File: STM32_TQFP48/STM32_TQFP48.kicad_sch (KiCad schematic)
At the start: 37 parts, among them SW1 SW_Push, SW2 SW_Push, U1 STM32L010C6Tx

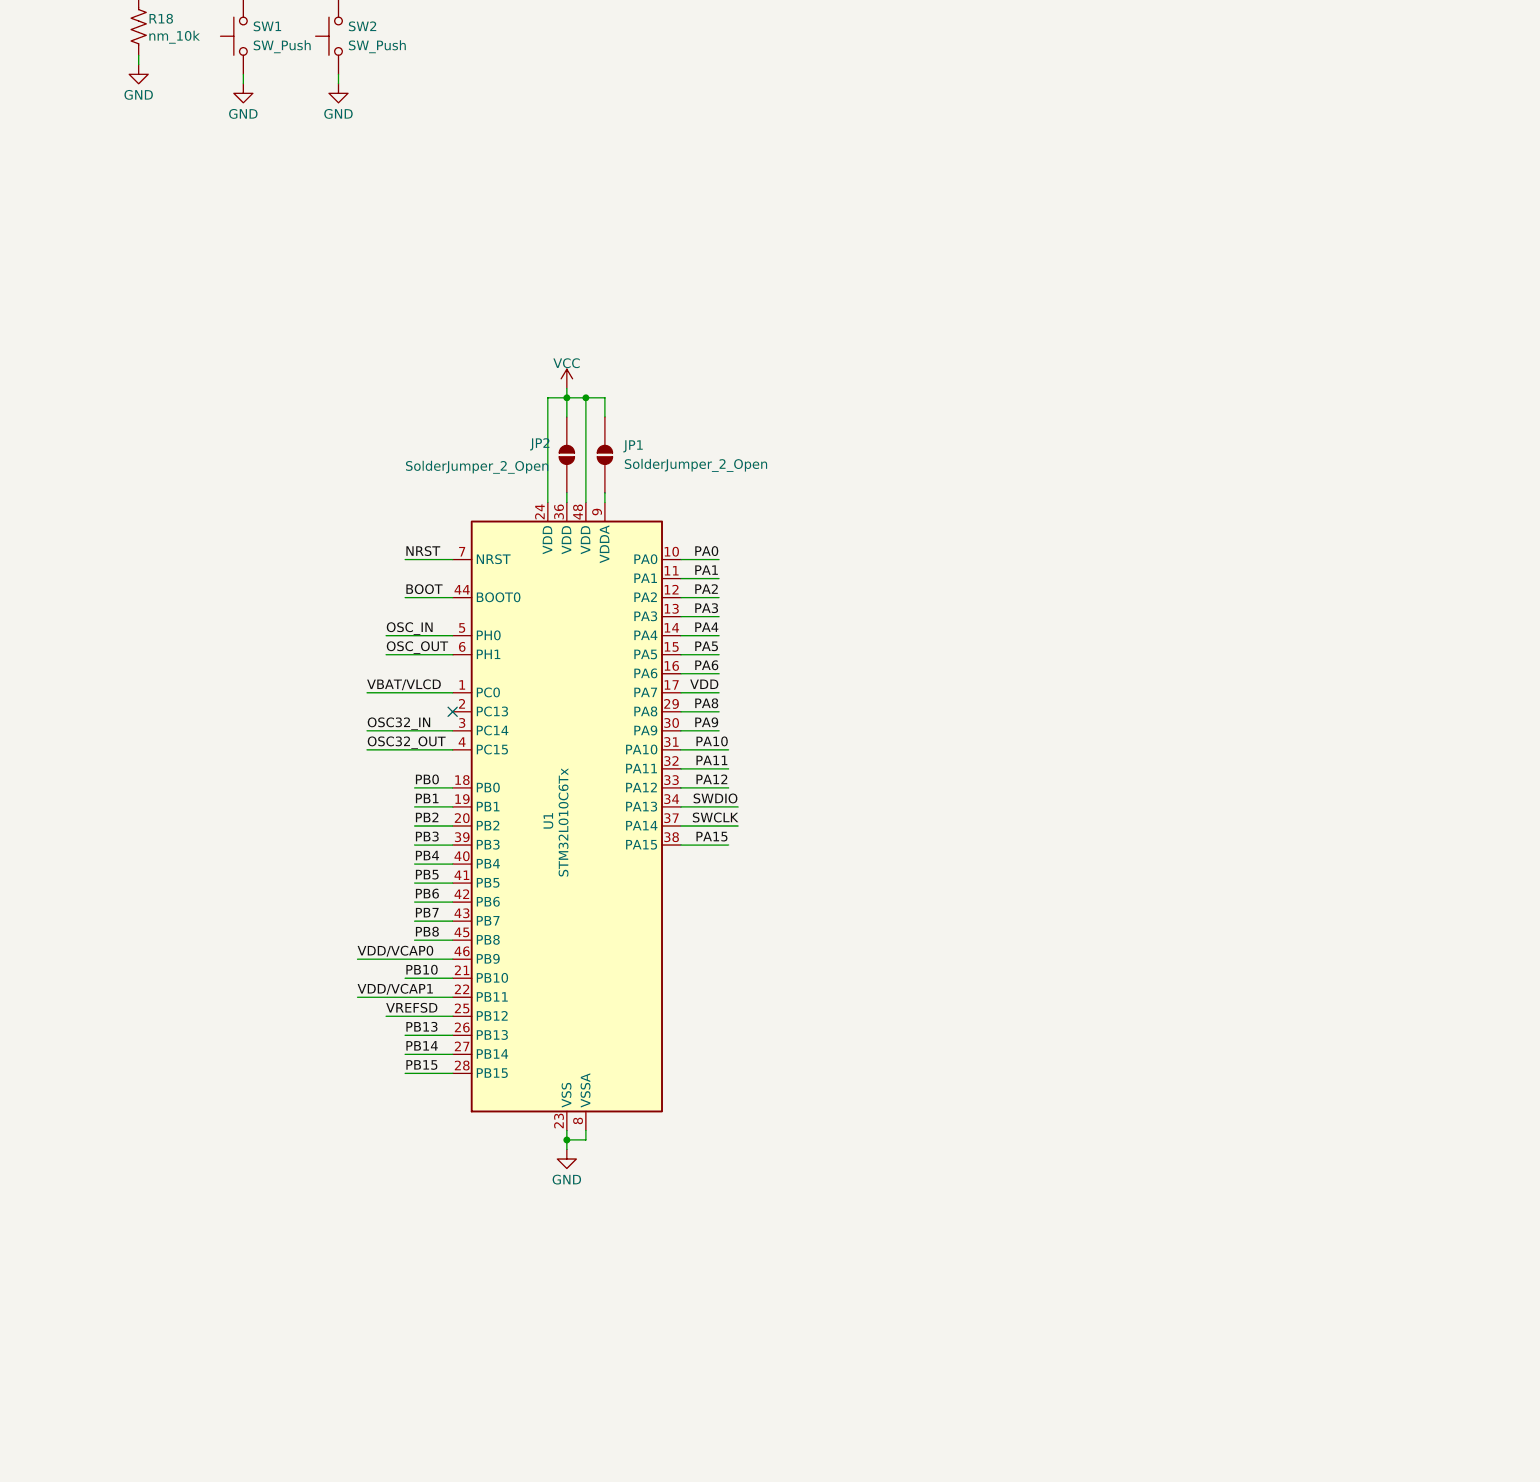
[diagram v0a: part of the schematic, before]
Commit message: STM32_TQFP48: Zaktualizowanie opisu konfiguracji pinoutu uC
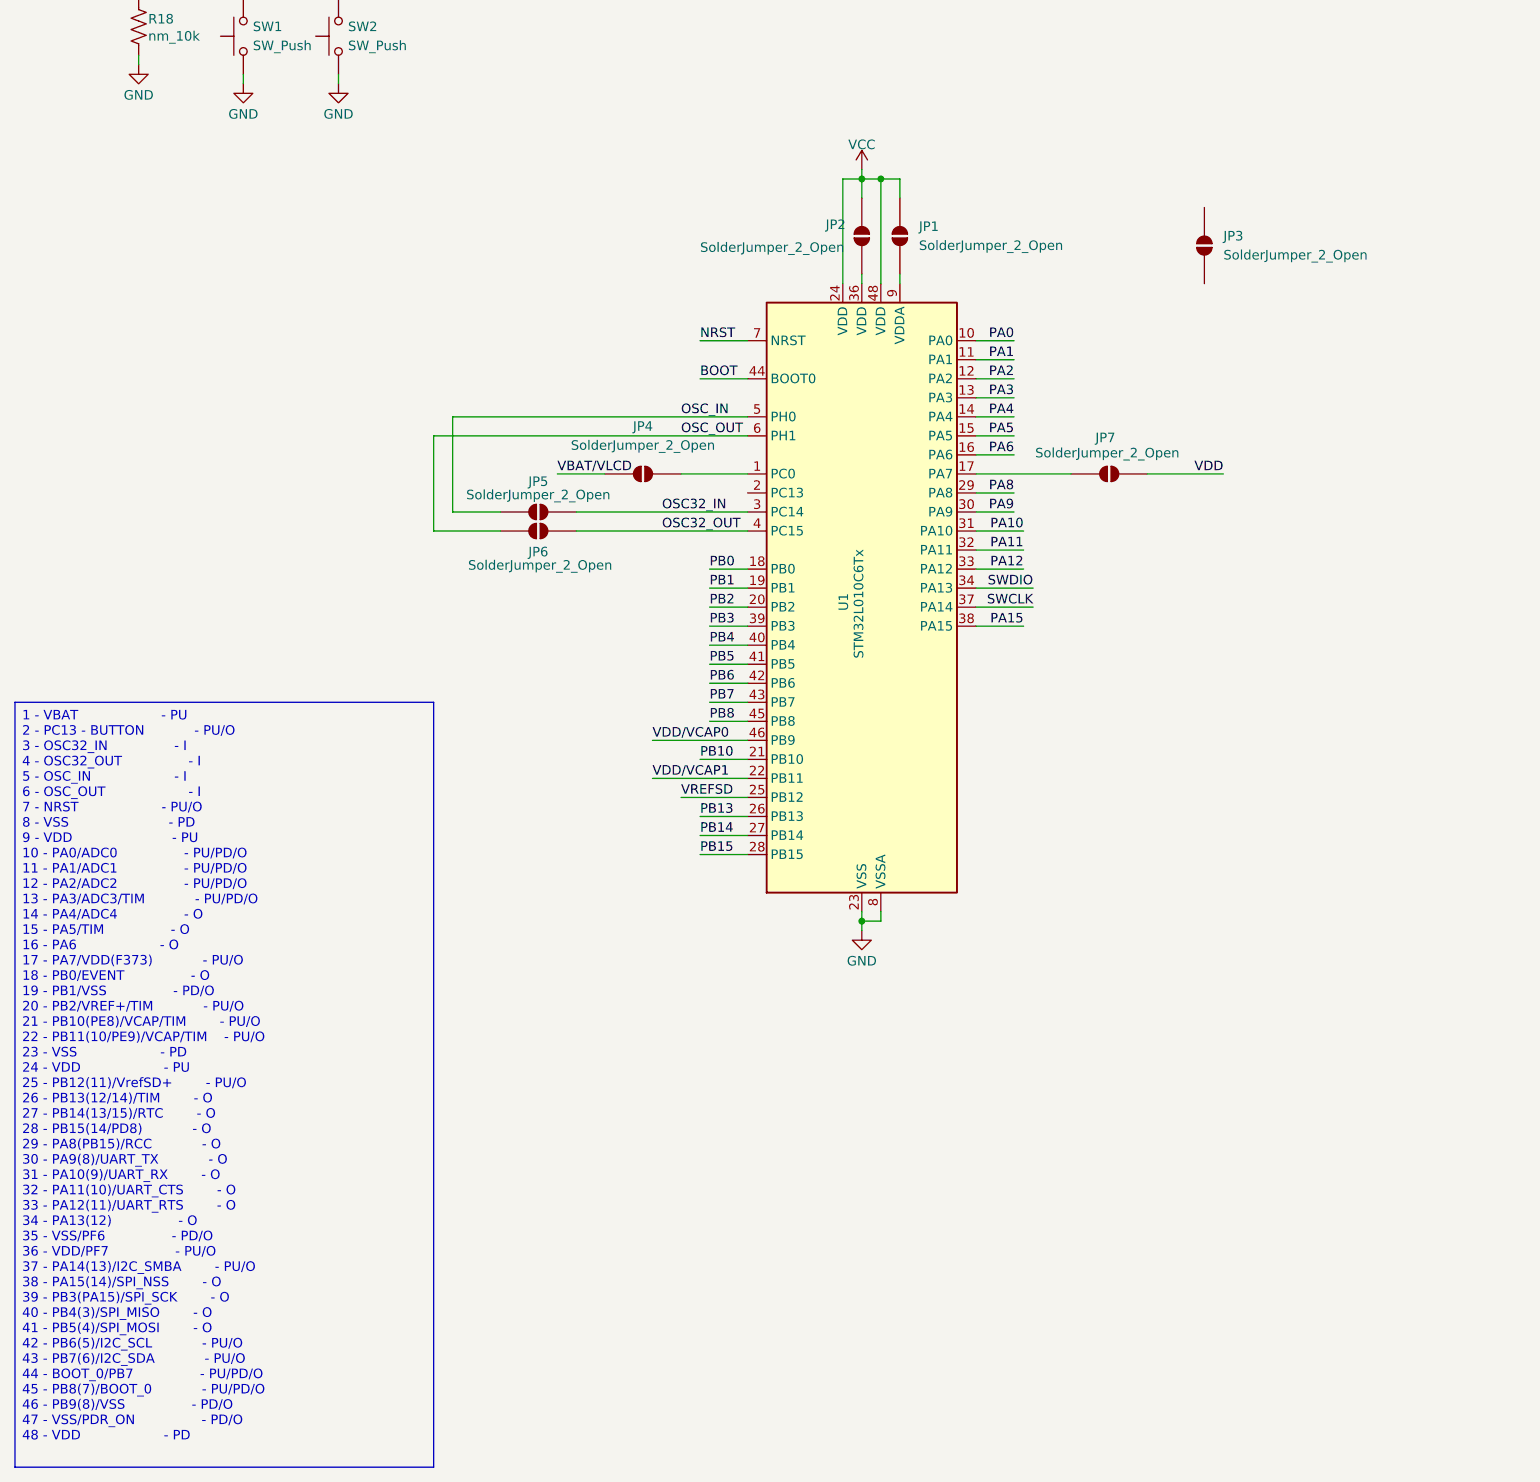
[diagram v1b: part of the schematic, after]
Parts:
- added JP3, JP4, JP5, JP6, JP7: SolderJumper_2_Open, symbol Jumper:SolderJumper_2_Open
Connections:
- net OSC32_IN: now also JP5.1 (A)
- net OSC32_OUT: now also JP6.1 (A)
- net OSC_IN: now also JP5.2 (B)
- net OSC_OUT: now also JP6.2 (B)
- net VBAT/VLCD: now also JP4.2 (B); no longer U1.1 (PC0)
- net VDD: now also JP7.1 (A); no longer U1.17 (PA7)
- new net: JP4.1 (A), U1.1 (PC0)
- new net: JP7.2 (B), U1.17 (PA7)
- no-connect marks 1 -> 0
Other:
- moved on the sheet: JP1, JP2, U1

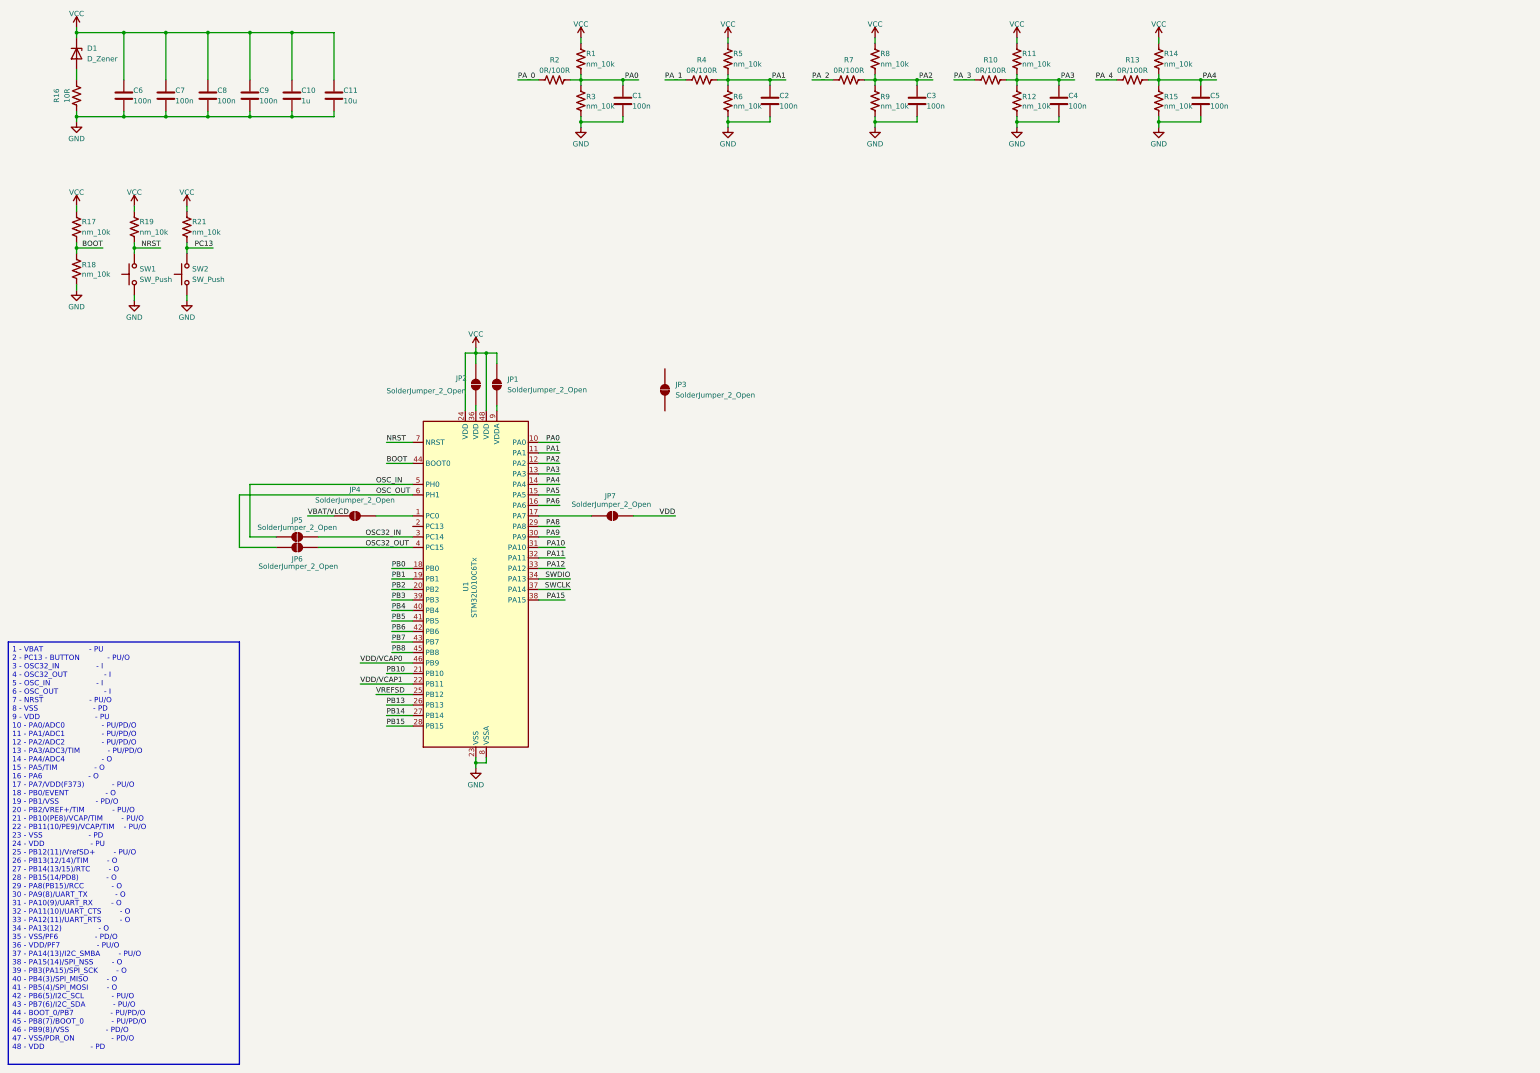
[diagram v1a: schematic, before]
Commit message: STM32_TQFP: Dalsza aktulizacja pinoutu, dodanie pierwszych układów wyprowadzeń.
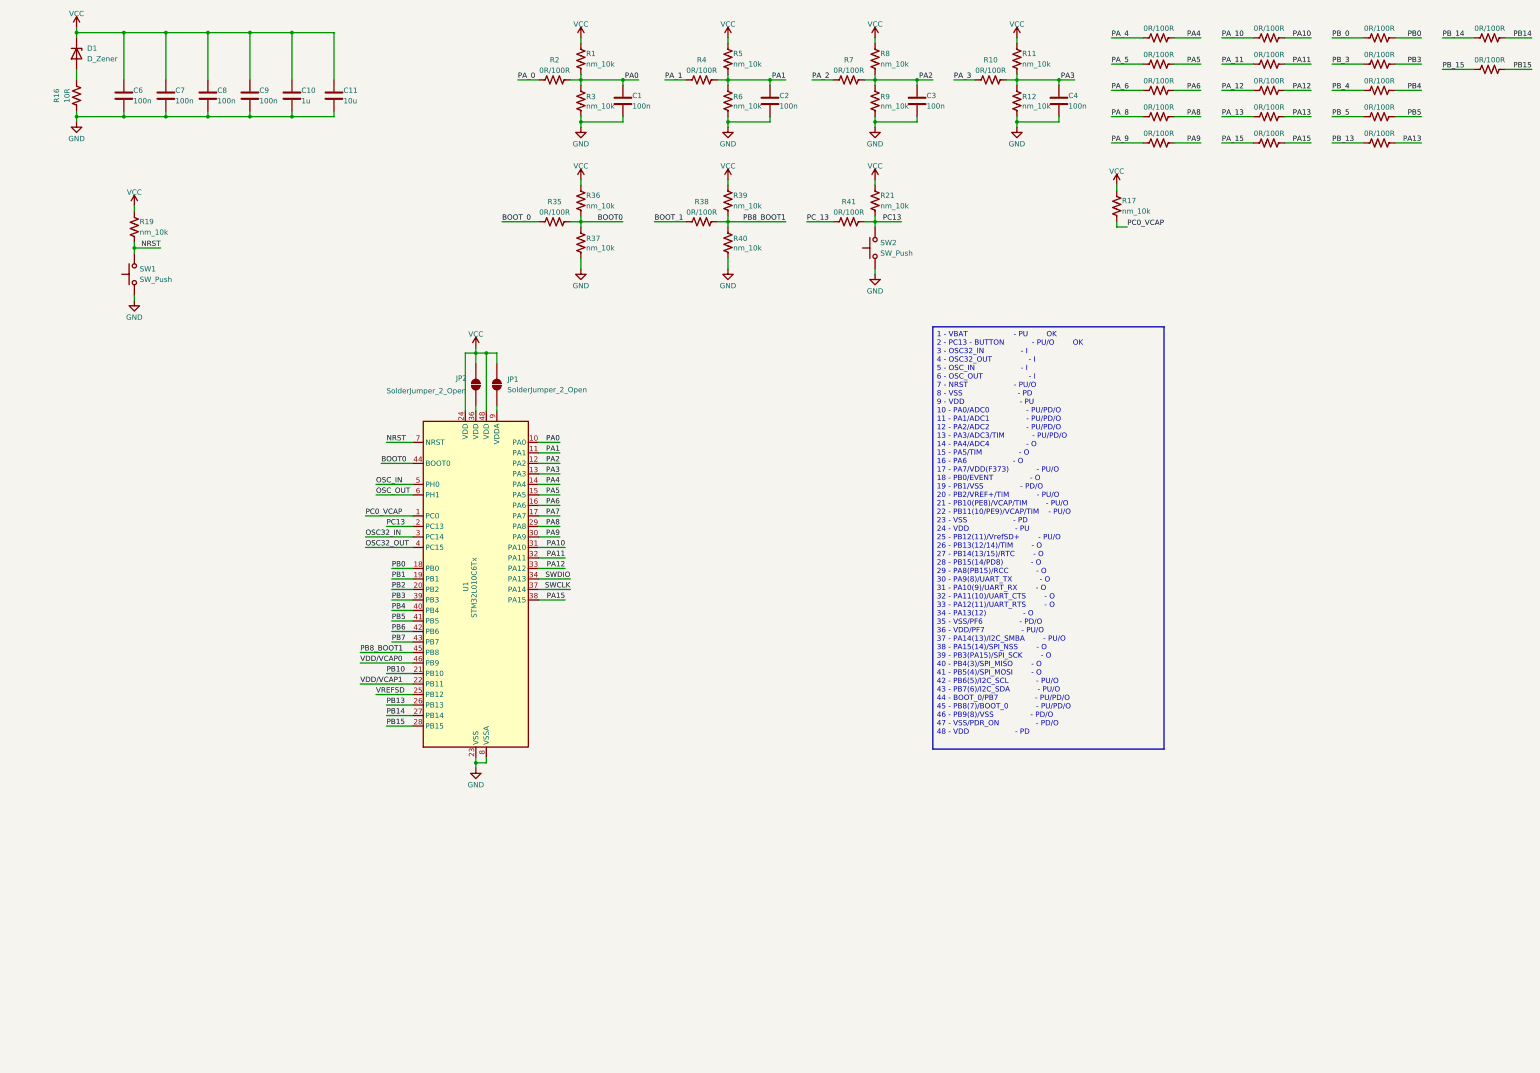
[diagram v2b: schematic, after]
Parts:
- removed C5: 100n, symbol Device:C
- removed JP3, JP4, JP5, JP6, JP7: SolderJumper_2_Open, symbol Jumper:SolderJumper_2_Open
- removed R18: nm_10k, symbol Device:R_US
- added R20, R22, R23, R24, R25, R26, R27, R28, R29, R30, R31, R32, R33, R34, R35, R38, R41: 0R/100R, symbol Device:R_US
- added R36, R37, R39, R40: nm_10k, symbol Device:R_US
- R14, R15: value nm_10k -> 0R/100R
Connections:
- net GND: now also R37.1, R40.1; no longer R15.1
- net PA10: now also R27.2
- net PA11: now also R28.2
- net PA12: now also R29.2
- net PA15: now also R31.2
- net PA4: no longer R14.2, R15.2
- net PA5: now also R14.2
- net PA6: now also R15.2
- net PA8: now also R25.2
- net PA9: now also R26.2
- net PB0: now also R20.2
- net PB14: now also R23.2
- net PB15: now also R24.2
- net PB3: now also R32.2
- net PB4: now also R33.2
- net PB5: now also R34.2
- net PC13: now also U1.2 (PC13), R41.2
- net VCC: now also R36.1, R39.1; no longer R14.1
- net PC0_VCAP: now reaches U1.1 (PC0)
- net PC0_VCAP: now also R17.2
- net PA7: now reaches U1.17 (PA7)
- net BOOT renamed BOOT0
- net BOOT0: now also R35.2, R36.2, R37.2; no longer R17.2
- net PB8 renamed PB8_BOOT1
- net PB8_BOOT1: now also R38.2, R39.2, R40.2
- new net BOOT_0: R35.1
- new net BOOT_1: R38.1
- new net PA13: R22.2, R30.2
- new net PA_10: R27.1
- new net PA_11: R28.1
- new net PA_12: R29.1
- new net PA_13: R30.1
- new net PA_15: R31.1
- new net PA_5: R14.1
- new net PA_6: R15.1
- new net PA_8: R25.1
- new net PA_9: R26.1
- new net PB_0: R20.1
- new net PB_13: R22.1
- new net PB_14: R23.1
- new net PB_15: R24.1
- new net PB_3: R32.1
- new net PB_4: R33.1
- new net PB_5: R34.1
- new net PC_13: R41.1

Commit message: STM32_TQFP48: Uporządkowanie i pogrupowanie elementów.
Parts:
- removed R13, R14, R15, R20, R22, R23, R24, R25, R26, R27, R28, R29, R30, R31, R32, R33, R34: 0R/100R, symbol Device:R_US
- added JP10, JP11, JP12, JP13, JP14, JP15, JP16, JP17, JP18, JP19, JP3, JP4, JP5, JP6, JP7, JP8, JP9: SolderJumper, symbol Jumper:SolderJumper_2_Open
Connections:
- net PA10: now also JP8.1 (A)
- net PA11: now also JP9.1 (A)
- net PA12: now also JP10.1 (A)
- net PA13: now also JP11.1 (A), JP17.1 (A)
- net PA15: now also JP12.1 (A)
- net PA4: now also JP3.1 (A)
- net PA5: now also JP4.1 (A)
- net PA6: now also JP5.1 (A)
- net PA8: now also JP6.1 (A)
- net PA9: now also JP7.1 (A)
- net PA_10: now also JP8.2 (B)
- net PA_11: now also JP9.2 (B)
- net PA_12: now also JP10.2 (B)
- net PA_13: now also JP11.2 (B)
- net PA_15: now also JP12.2 (B)
- net PA_4: now also JP3.2 (B)
- net PA_5: now also JP4.2 (B)
- net PA_6: now also JP5.2 (B)
- net PA_8: now also JP6.2 (B)
- net PA_9: now also JP7.2 (B)
- net PB0: now also JP13.1 (A)
- net PB14: now also JP19.1 (A)
- net PB15: now also JP18.1 (A)
- net PB3: now also JP14.1 (A)
- net PB4: now also JP15.1 (A)
- net PB5: now also JP16.1 (A)
- net PB_0: now also JP13.2 (B)
- net PB_13: now also JP17.2 (B)
- net PB_14: now also JP19.2 (B)
- net PB_15: now also JP18.2 (B)
- net PB_3: now also JP14.2 (B)
- net PB_4: now also JP15.2 (B)
- net PB_5: now also JP16.2 (B)
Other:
- note added: "Analog pins"
- note added: "Boot Options"
- note added: "Buttons"
- note added: "GPIO"
- note added: "Power pins"
- note added: "Power supply section"
- moved on the sheet: C1, C10, C11, C2, C3, C4, C6, C7, C8, C9, D1, JP1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

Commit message: STM32_TQFP48: Dodanie sekcji: Power pin, Optional power pin, Oscillator i Programming socket
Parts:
- removed JP1, JP2: SolderJumper_2_Open, symbol Jumper:SolderJumper_2_Open
- added C12, C5: C, symbol Device:C
- added JP20, JP21, JP22, JP23, JP24, JP25, JP26, JP27, JP28: SolderJumper, symbol Jumper:SolderJumper_2_Open
- added R13, R15, R20, R23, R25, R27: 0R/100R, symbol Device:R_US
- added R14, R18, R22, R24, R26, R28, R29: nm_10k, symbol Device:R_US
- added Y1: Crystal, symbol Device:Crystal
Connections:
- net PA_13 is gone; now on net P9: JP11.2 (B)
- net GND: now also C12.2, C5.2, JP27.1 (A), JP28.1 (A), R18.1, R29.2; no longer U1.23 (VSS), U1.35 (VSS), U1.47 (VSS), U1.8 (VSSA)
- net OSC32_IN: now also JP23.2 (B)
- net OSC32_OUT: now also JP21.1 (A)
- net OSC_IN: now also JP22.2 (B)
- net OSC_OUT: now also JP20.1 (A)
- net PA13: no longer JP11.1 (A)
- net VCC: now also JP11.1 (A), JP24.1 (A), JP25.2 (B), JP26.1 (A), R14.1, R22.1, R24.1, R26.1, R28.1; no longer U1.24 (VDD), U1.48 (VDD)
- net P36: now reaches U1.36 (VDD)
- net P36: now also JP25.1 (A), R29.1
- net P9: now reaches U1.9 (VDDA)
- net PA7 renamed PA7/VDD
- net PA7/VDD: now also R13.2, R14.2
- net PB1 renamed PB1/VSS
- net PB1/VSS: now also R15.2, R18.2
- net PB10 renamed PB10/VCAP
- net PB10/VCAP: now also R23.2, R24.2
- net PB2 renamed PB2/VREF+
- net PB2/VREF+: now also R20.2, R22.2
- net SWCLK renamed PA14/SWCLK
- net SWDIO renamed PA13/SWDIO
- net VDD/VCAP1 renamed PB11/VDD/VCAP
- net PB11/VDD/VCAP: now also R25.2, R26.2
- net VREFSD renamed PB12/VREFSD+
- net PB12/VREFSD+: now also R27.2, R28.2
- new net OscIn: C5.1, JP22.1 (A), JP23.1 (A), Y1.1
- new net OscOut: C12.1, JP20.2 (B), JP21.2 (B), Y1.2
- new net P23: JP28.2 (B), U1.23 (VSS), U1.35 (VSS), U1.47 (VSS)
- new net P24: JP24.2 (B), U1.24 (VDD)
- new net P48: JP26.2 (B), U1.48 (VDD)
- new net P8: JP27.2 (B), U1.8 (VSSA)
- new net PA_7: R13.1
- new net PB_1: R15.1
- new net PB_10: R23.1
- new net PB_11: R25.1
- new net PB_12: R27.1
- new net PB_2: R20.1
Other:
- note added: "Optional Power pins"
- note added: "Oscillator"
- note added: "Programming socket"
- moved on the sheet: JP12, R17, R19, R21, R41, SW1, SW2
